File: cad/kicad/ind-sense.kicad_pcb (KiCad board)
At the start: 2 copper layers, 61 parts, among them J1 Conn_01x27, J2 Conn_01x27, J3 Conn_01x18, U1 74HC154, U2 MCP4821, U5 CMP04, U6 CMP04

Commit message: updaded board and added some further documentation for egineering desicions, need to add further documentation to help people get up to speed with the project
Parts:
- moved J2 241.0 mm to (40.7, 35.0), turned to 90 degrees
- moved L4 236.9 mm to (50.2, 105.0)
- moved L11 230.3 mm to (88.2, 85.9)
- moved L20 227.5 mm to (126.4, 104.9)
- moved L19 225.1 mm to (126.4, 85.8)
- moved L2 223.5 mm to (50.2, 66.8)
- moved L10 218.8 mm to (88.2, 66.8)
- moved L18 216.5 mm to (126.4, 66.8)
- moved L1 215.7 mm to (50.2, 47.8)
- moved L7 215.5 mm to (69.2, 85.9)
- moved L3 212.8 mm to (50.2, 85.9)
- moved L9 209.0 mm to (88.2, 47.7)
- moved L12 208.5 mm to (88.2, 105.0)
- moved L5 208.0 mm to (69.2, 47.7)
- moved L8 204.5 mm to (69.2, 105.0)
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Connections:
- J2 pad 10: /matrix/MRP8 -> /matrix/MRP1
- J2 pad 3: /matrix/MRP1 -> /matrix/MRP8
- J2 pad 4: /matrix/MRP2 -> /matrix/MRP4
- J2 pad 5: /matrix/MRP3 -> /matrix/MRP7
- J2 pad 6: /matrix/MRP4 -> /matrix/MRP3
- J2 pad 7: /matrix/MRP5 -> /matrix/MRP6
- J2 pad 8: /matrix/MRP6 -> /matrix/MRP2
- J2 pad 9: /matrix/MRP7 -> /matrix/MRP5
- J3 pad 2: ~SS -> SDI
- J3 pad 4: SDI -> ~SS
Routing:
- net /matrix/MCN4: track 0.00 -> 324.7 mm, vias 0 -> 5
- net /matrix/MCN3: track 0.00 -> 316.1 mm, vias 0 -> 5
- net /matrix/MRP8: track 0.00 -> 297.0 mm
- net /matrix/MCN2: track 0.00 -> 288.8 mm, vias 0 -> 1
- net /matrix/MRP7: track 0.00 -> 284.0 mm
- net /matrix/MCN1: track 0.00 -> 279.2 mm, vias 0 -> 1
- net /matrix/MRP6: track 0.00 -> 261.7 mm
- net /matrix/MRP5: track 0.00 -> 238.7 mm
- net /matrix/MRP4: track 0.00 -> 218.1 mm
- net /matrix/MRP3: track 0.00 -> 202.4 mm
- net /matrix/MRP2: track 0.00 -> 179.7 mm
- net /matrix/MRP1: track 0.00 -> 158.1 mm
- net GNDREF: track 0.00 -> 57.7 mm
- net SP: track 133.5 -> 89.4 mm, vias 5 -> 4
- net GND: track 275.4 -> 295.0 mm, vias 15 -> 17
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- added copper zone on B.Cu, net GNDREF
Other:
- board outline added: 162.4 x 85.1 mm

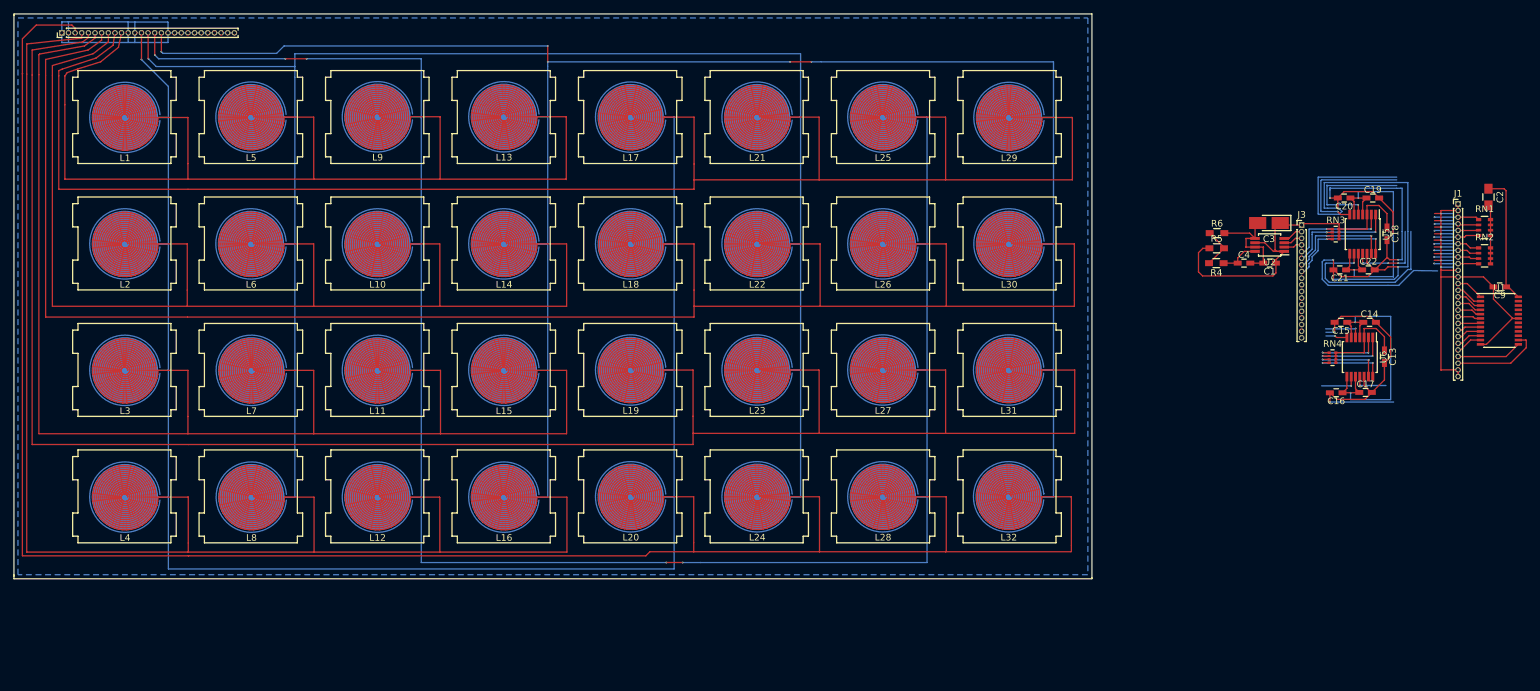
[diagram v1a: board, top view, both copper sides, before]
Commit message: added logo, and started work on panelizing the demo pcb
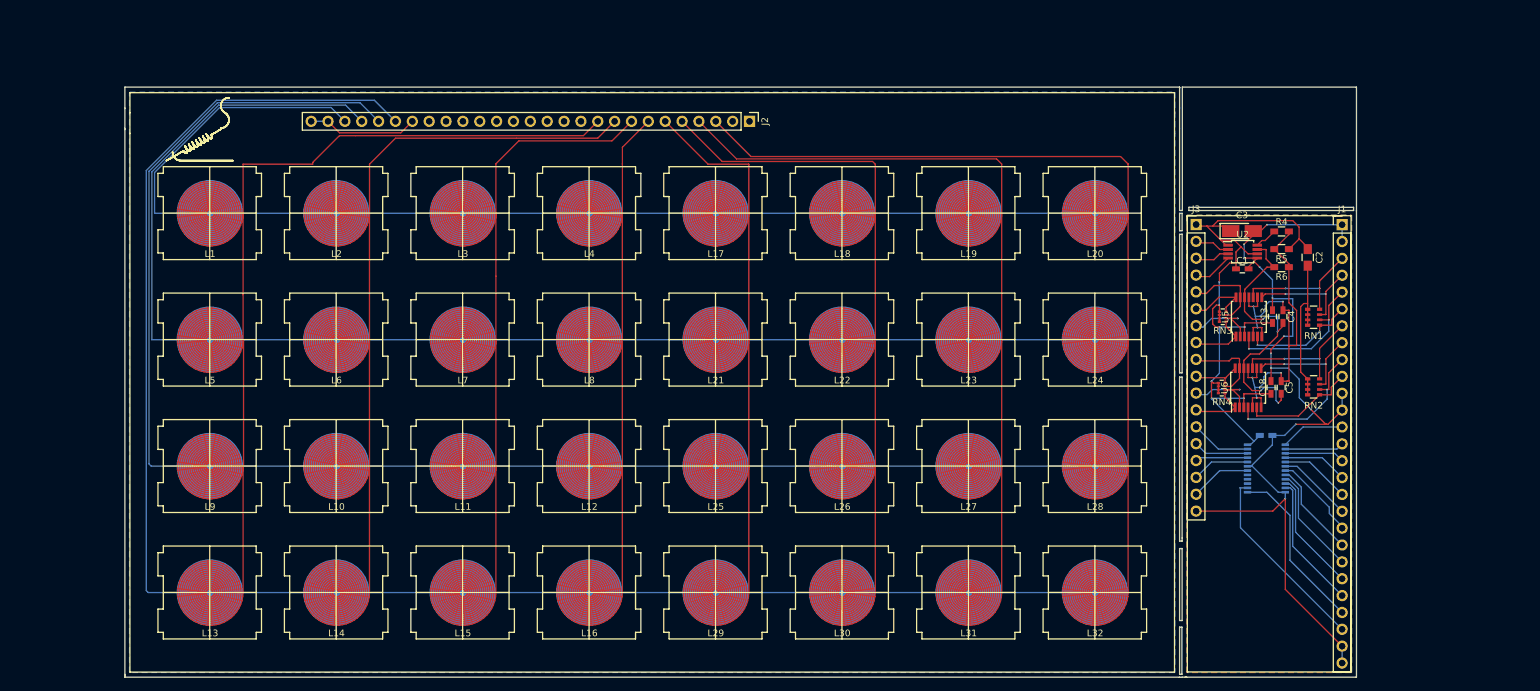
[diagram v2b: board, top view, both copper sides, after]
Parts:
- removed C14, C15, C16, C17, C19, C20, C21, C22: 0u1, Capacitors_SMD:C_0603_HandSoldering
- added C5: 1u, Capacitors_SMD:C_0603_HandSoldering, F.Cu at (224.4, 88.4)
- C9, U1: moved to B.Cu
- J1, J2: footprint Pin_Headers:Pin_Header_Straight_1x27_Pitch1.00mm -> Pin_Headers:Pin_Header_Straight_1x27_Pitch2.54mm
- J3: footprint Pin_Headers:Pin_Header_Straight_1x18_Pitch1.00mm -> Pin_Headers:Pin_Header_Straight_1x18_Pitch2.54mm
- moved J2 104.5 mm to (144.3, 48.3), turned to 270 degrees
- moved L13 84.3 mm to (63.0, 119.3)
- moved L29 84.1 mm to (139.2, 119.3)
- moved L4 82.0 mm to (120.1, 62.2)
- moved L20 82.0 mm to (196.3, 62.2)
- moved L9 58.4 mm to (63.0, 100.3)
- moved L25 58.3 mm to (139.2, 100.3)
- moved L14 58.3 mm to (82.0, 119.3)
- moved L30 58.2 mm to (158.2, 119.3)
- moved L8 56.2 mm to (120.1, 81.2)
- moved L24 56.1 mm to (196.3, 81.2)
- moved L3 56.1 mm to (101.1, 62.2)
- moved L19 56.1 mm to (177.3, 62.2)
- moved C9 41.7 mm to (222.1, 95.7), turned to 0 degrees
- moved U1 41.6 mm to (222.2, 100.6), turned to 180 degrees
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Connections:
- C4 pad 1: Net-(C4-Pad1) -> SP
- J2 pad 13: /matrix/MCN1 -> GNDREF
- J2 pad 14: /matrix/MCN2 -> GNDREF
- J2 pad 15: /matrix/MCN3 -> GNDREF
- J2 pad 16: /matrix/MCN4 -> GNDREF
- J2 pad 22: GNDREF -> /matrix/MCN10
- J2 pad 23: GNDREF -> /matrix/MCN11
- J2 pad 24: GNDREF -> /matrix/MCN12
- J2 pad 25: GNDREF -> /matrix/MCN13
- J2 pad 4: /matrix/MRP4 -> /matrix/MRP7
- J2 pad 5: /matrix/MRP7 -> /matrix/MRP6
- J2 pad 6: /matrix/MRP3 -> /matrix/MRP5
- J2 pad 7: /matrix/MRP6 -> /matrix/MRP4
- J2 pad 8: /matrix/MRP2 -> /matrix/MRP3
- J2 pad 9: /matrix/MRP5 -> /matrix/MRP2
- J3 pad 2: SDI -> ~SS
- J3 pad 4: ~SS -> SDI
- L1 pad 2: /matrix/MCN1 -> /matrix/MCN13
- L10 pad 2: /matrix/MCN3 -> /matrix/MCN11
- L11 pad 2: /matrix/MCN3 -> /matrix/MCN11
- L12 pad 2: /matrix/MCN3 -> /matrix/MCN11
- L13 pad 2: /matrix/MCN4 -> /matrix/MCN10
- L14 pad 2: /matrix/MCN4 -> /matrix/MCN10
- L15 pad 2: /matrix/MCN4 -> /matrix/MCN10
- L16 pad 2: /matrix/MCN4 -> /matrix/MCN10
- L17 pad 2: /matrix/MCN1 -> /matrix/MCN13
- L18 pad 2: /matrix/MCN1 -> /matrix/MCN13
- L19 pad 2: /matrix/MCN1 -> /matrix/MCN13
- L2 pad 2: /matrix/MCN1 -> /matrix/MCN13
- L20 pad 2: /matrix/MCN1 -> /matrix/MCN13
- L21 pad 2: /matrix/MCN2 -> /matrix/MCN12
- L22 pad 2: /matrix/MCN2 -> /matrix/MCN12
- L23 pad 2: /matrix/MCN2 -> /matrix/MCN12
- L24 pad 2: /matrix/MCN2 -> /matrix/MCN12
- L25 pad 2: /matrix/MCN3 -> /matrix/MCN11
- L26 pad 2: /matrix/MCN3 -> /matrix/MCN11
- L27 pad 2: /matrix/MCN3 -> /matrix/MCN11
- L28 pad 2: /matrix/MCN3 -> /matrix/MCN11
- L29 pad 2: /matrix/MCN4 -> /matrix/MCN10
- L3 pad 2: /matrix/MCN1 -> /matrix/MCN13
- L30 pad 2: /matrix/MCN4 -> /matrix/MCN10
- L31 pad 2: /matrix/MCN4 -> /matrix/MCN10
- L32 pad 2: /matrix/MCN4 -> /matrix/MCN10
- L4 pad 2: /matrix/MCN1 -> /matrix/MCN13
- L5 pad 2: /matrix/MCN2 -> /matrix/MCN12
- L6 pad 2: /matrix/MCN2 -> /matrix/MCN12
- L7 pad 2: /matrix/MCN2 -> /matrix/MCN12
- L8 pad 2: /matrix/MCN2 -> /matrix/MCN12
- L9 pad 2: /matrix/MCN3 -> /matrix/MCN11
- R4 pad 1: Net-(C4-Pad1) -> Net-(R4-Pad1)
- RN1 pad 1: M1 -> M4
- RN1 pad 2: M2 -> M3
- RN1 pad 3: M3 -> M2
- RN1 pad 4: M4 -> M1
- RN2 pad 1: M5 -> M8
- RN2 pad 2: M6 -> M7
- RN2 pad 3: M7 -> M6
- RN2 pad 4: M8 -> M5
- RN3 pad 1: S1 -> S4
- RN3 pad 2: S2 -> S3
- RN3 pad 3: S3 -> S1
- RN3 pad 4: S4 -> S2
- RN4 pad 1: S5 -> S8
- RN4 pad 2: S6 -> S7
- RN4 pad 3: S7 -> S5
- RN4 pad 4: S8 -> S6
- U1 pad 15: Net-(U1-Pad15) -> (no net)
- U1 pad 16: Net-(U1-Pad16) -> (no net)
- U1 pad 17: Net-(U1-Pad17) -> (no net)
- U2 pad 8: Net-(C4-Pad1) -> Net-(R4-Pad1)
- U5 pad 1: S2 -> S4
- U5 pad 10: SP -> M1
- U5 pad 11: M3 -> SP
- U5 pad 13: S3 -> S1
- U5 pad 14: S4 -> S2
- U5 pad 2: S1 -> S3
- U5 pad 4: SP -> M3
- U5 pad 5: M1 -> SP
- U5 pad 6: SP -> M4
- U5 pad 7: M2 -> SP
- U5 pad 8: SP -> M2
- U5 pad 9: M4 -> SP
- U6 pad 1: S6 -> S8
- U6 pad 10: SP -> M5
- U6 pad 11: M7 -> SP
- U6 pad 13: S7 -> S5
- U6 pad 14: S8 -> S6
- U6 pad 2: S5 -> S7
- U6 pad 4: SP -> M7
- U6 pad 5: M5 -> SP
- U6 pad 6: SP -> M8
- U6 pad 7: M6 -> SP
- U6 pad 8: SP -> M6
- U6 pad 9: M8 -> SP
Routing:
- net /matrix/MCN4: track 324.7 -> 0.00 mm, vias 5 -> 0
- net /matrix/MCN3: track 316.1 -> 0.00 mm, vias 5 -> 0
- net /matrix/MCN2: track 288.8 -> 0.00 mm, vias 1 -> 0
- net /matrix/MCN1: track 279.2 -> 0.00 mm, vias 1 -> 0
- net /matrix/MCN10: track 0.00 -> 249.7 mm
- net /matrix/MCN11: track 0.00 -> 229.4 mm
- net /matrix/MCN12: track 0.00 -> 208.8 mm
- net /matrix/MCN13: track 0.00 -> 181.4 mm
- net /matrix/MRP7: track 284.0 -> 112.9 mm
- net /matrix/MRP8: track 297.0 -> 129.3 mm
- net /matrix/MRP6: track 261.7 -> 96.3 mm
- net /matrix/MRP5: track 238.7 -> 79.8 mm
- net /matrix/MRP4: track 218.1 -> 72.6 mm
- net /matrix/MRP3: track 202.4 -> 87.7 mm
- net GND: track 295.0 -> 181.1 mm, vias 17 -> 15
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- added copper zone on B.Cu, net GND
- added copper zone on F.Cu, net GND
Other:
- board size 162.4 x 85.1 mm -> 185.5 x 88.9 mm
